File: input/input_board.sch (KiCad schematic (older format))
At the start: 21 parts, among them J2 SCKB, J4 SCKA, J5 MCLK, J6 SDOB1, U1 DS90LV048, U2 FIN1047, U5 74LVC541A

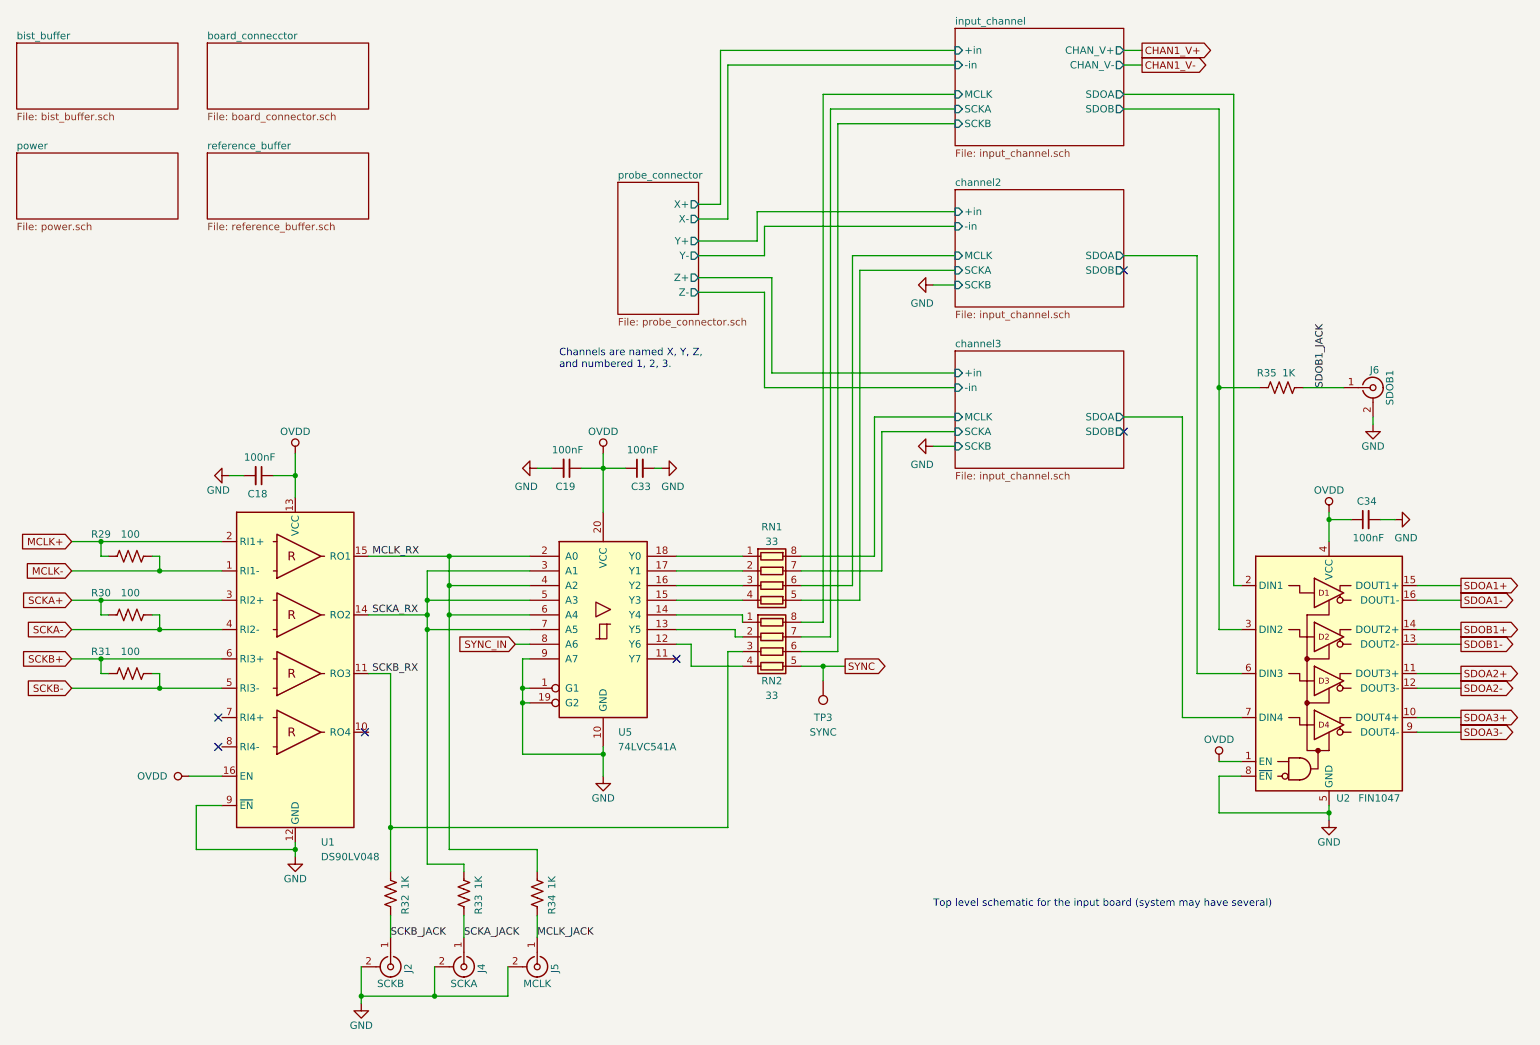
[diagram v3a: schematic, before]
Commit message: Input board is nearly ready to send off for the first spin.
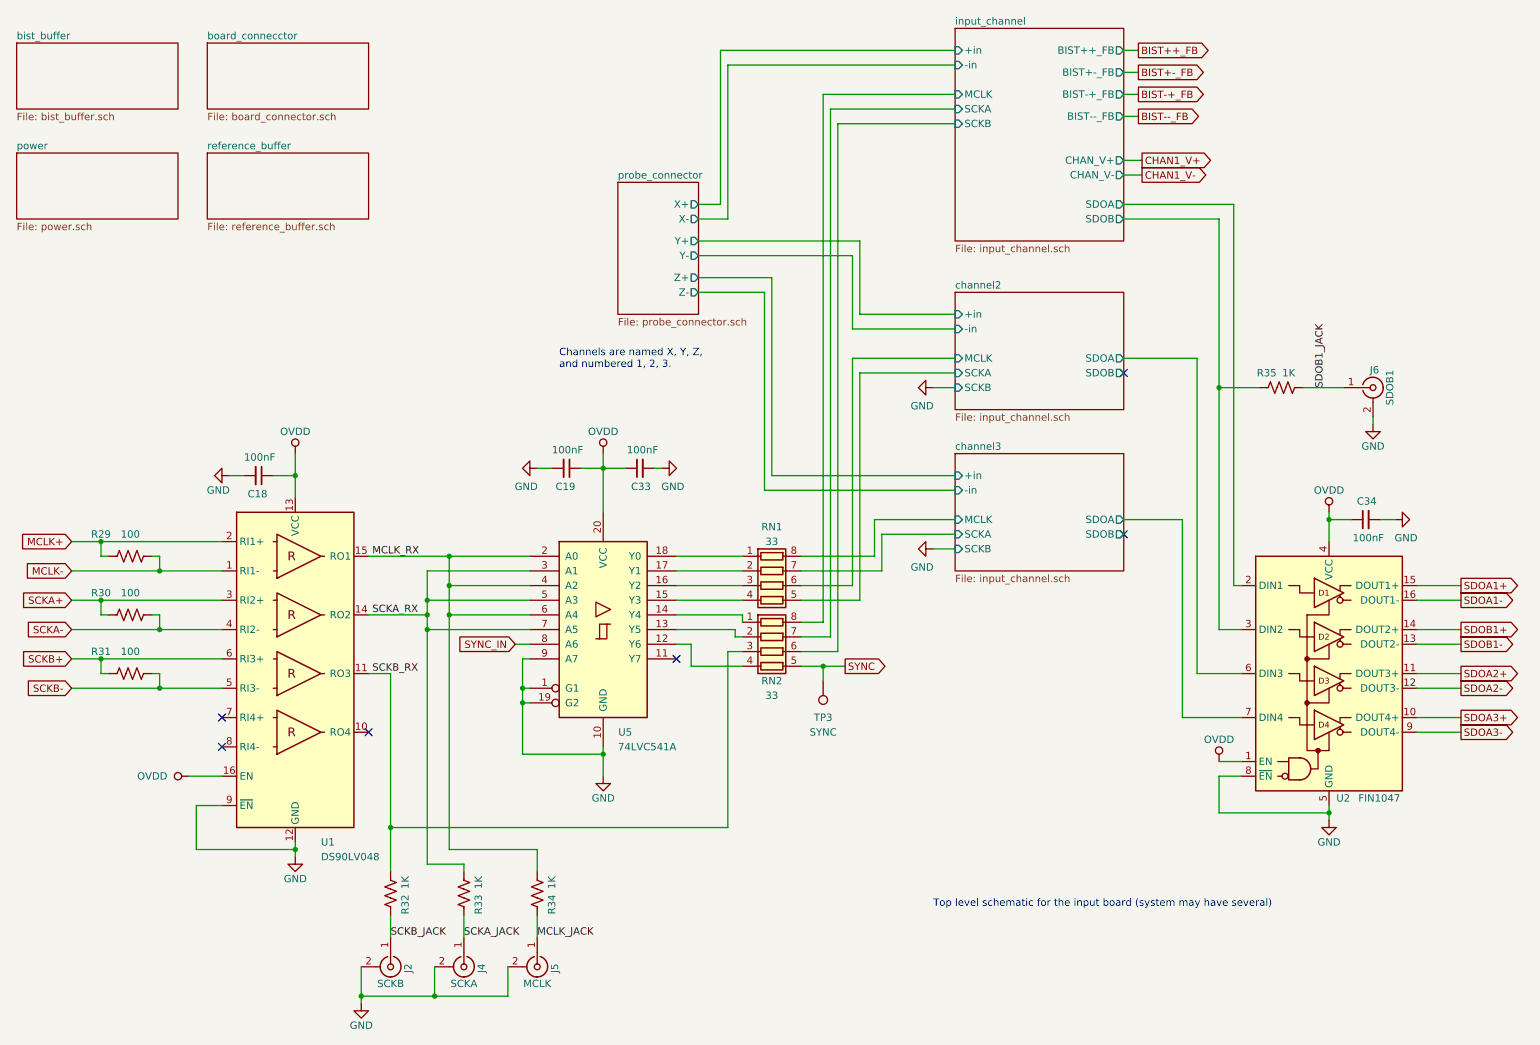
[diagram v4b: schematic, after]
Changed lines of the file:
@@
 $EndComp
-$Sheet
-S 7300 850  1150 800
-U 5DFCF14D
-F0 "input_channel" 50
-F1 "input_channel.sch" 50
-F2 "+in" I L 7300 1000 50
-F3 "-in" I L 7300 1100 50
-F4 "SDOA" O R 8450 1300 50
-F5 "SDOB" O R 8450 1400 50
-F6 "MCLK" I L 7300 1300 50
-F7 "SCKB" I L 7300 1500 50
-F8 "SCKA" I L 7300 1400 50
-F9 "CHAN_V+" O R 8450 1000 50
-F10 "CHAN_V-" O R 8450 1100 50
-$EndSheet
 $Sheet
 S 2200 950  1100 450
@@
 Text GLabel 6550 5200 2    50   Output ~ 0
 SYNC
-NoConn ~ 3275 5650
-NoConn ~ 2275 5750
-NoConn ~ 2275 5550
+NoConn ~ 3300 5650
+NoConn ~ 2300 5750
+NoConn ~ 2300 5550
 Text Notes 7150 6850 0    50   ~ 0
 Top level schematic for the input board (system may have several)
@@
 $EndSheet
 Wire Wire Line
-	8450 1300 9200 1300
-Wire Wire Line
-	9200 1300 9200 4650
-Wire Wire Line
 	9200 4650 9250 4650
 Wire Wire Line
-	8450 1400 9100 1400
-Wire Wire Line
-	9100 1400 9100 3300
-Wire Wire Line
 	9100 4950 9250 4950
 Wire Wire Line
 	9250 5250 8950 5250
 Wire Wire Line
-	8950 5250 8950 2400
-Wire Wire Line
-	8950 2400 8450 2400
+	8950 5250 8950 3100
 Wire Wire Line
 	9250 5550 8850 5550
 Wire Wire Line
-	8850 5550 8850 3500
-Wire Wire Line
-	8850 3500 8450 3500
-NoConn ~ 8450 2500
+	8850 5550 8850 4200
+NoConn ~ 8450 3200
 Wire Wire Line
 	5550 2050 5700 2050
@@
 	5700 2050 5700 1000
 Wire Wire Line
-	5700 1000 7300 1000
-Wire Wire Line
 	5750 2150 5750 1100
 Wire Wire Line
-	5750 1100 7300 1100
-Wire Wire Line
 	5550 2150 5750 2150
 Wire Wire Line
-	5550 2300 5950 2300
-Wire Wire Line
-	5950 2300 5950 2100
-Wire Wire Line
-	5950 2100 7300 2100
-Wire Wire Line
-	5550 2400 6000 2400
-Wire Wire Line
-	6000 2400 6000 2200
-Wire Wire Line
-	6000 2200 7300 2200
-Wire Wire Line
 	5550 2550 6050 2550
 Wire Wire Line
-	6050 2550 6050 3200
-Wire Wire Line
-	6050 3200 7300 3200
-Wire Wire Line
 	5550 2650 6000 2650
-Wire Wire Line
-	6000 2650 6000 3300
-Wire Wire Line
-	6000 3300 7300 3300
 $Comp
 L power:GND #PWR0131
@@
 L power:GND #PWR0147
 U 1 1 5E2F0AE0
-P 7150 3700
-F 0 "#PWR0147" H 7150 3450 50  0001 C CNN
-F 1 "GND" V 7275 3625 50  0000 C CNN
-F 2 "" H 7150 3700 50  0001 C CNN
-F 3 "" H 7150 3700 50  0001 C CNN
-	1    7150 3700
+P 7150 4400
+F 0 "#PWR0147" H 7150 4150 50  0001 C CNN
+F 1 "GND" V 7275 4325 50  0000 C CNN
+F 2 "" H 7150 4400 50  0001 C CNN
+F 3 "" H 7150 4400 50  0001 C CNN
+	1    7150 4400
 	0    1    1    0
 $EndComp
@@
 L power:GND #PWR0146
 U 1 1 5E2EC6DB
-P 7150 2600
-F 0 "#PWR0146" H 7150 2350 50  0001 C CNN
-F 1 "GND" V 7275 2525 50  0000 C CNN
-F 2 "" H 7150 2600 50  0001 C CNN
-F 3 "" H 7150 2600 50  0001 C CNN
-	1    7150 2600
+P 7150 3300
+F 0 "#PWR0146" H 7150 3050 50  0001 C CNN
+F 1 "GND" V 7275 3225 50  0000 C CNN
+F 2 "" H 7150 3300 50  0001 C CNN
+F 3 "" H 7150 3300 50  0001 C CNN
+	1    7150 3300
 	0    1    1    0
 $EndComp
 Wire Wire Line
-	7150 2600 7300 2600
-Wire Wire Line
-	7150 3700 7300 3700
-Wire Wire Line
-	7300 1300 6400 1300
-Wire Wire Line
-	7300 1400 6450 1400
-Wire Wire Line
-	7300 1500 6500 1500
+	7150 3300 7300 3300
+Wire Wire Line
+	7150 4400 7300 4400
 Wire Wire Line
 	5400 4450 5850 4450
@@
 	3450 5250 3450 6300
 Wire Wire Line
-	7300 2400 6600 2400
-Wire Wire Line
-	7300 2500 6650 2500
-Wire Wire Line
-	7300 3500 6750 3500
-Wire Wire Line
-	6750 3500 6750 4450
-Wire Wire Line
-	7300 3600 6800 3600
-Wire Wire Line
 	6400 4900 6250 4900
 Wire Wire Line
@@
 	6600 4650 6250 4650
 Wire Wire Line
-	6600 2400 6600 4650
-Wire Wire Line
 	6650 4750 6250 4750
 Wire Wire Line
-	6650 2500 6650 4750
-Wire Wire Line
 	6250 4450 6750 4450
 Wire Wire Line
 	6250 4550 6800 4550
-Wire Wire Line
-	6800 3600 6800 4550
 Text Label 3450 7050 0    50   ~ 0
 SCKB_JACK
@@
 Text Label 9825 3300 1    50   ~ 0
 SDOB1_JACK
-Text GLabel 8575 1000 2    50   Output ~ 0
+Text GLabel 8575 1750 2    50   Output ~ 0
 CHAN1_V+
-Text GLabel 8575 1100 2    50   Output ~ 0
+Text GLabel 8575 1850 2    50   Output ~ 0
 CHAN1_V-
 Wire Wire Line
-	8575 1000 8450 1000
-Wire Wire Line
-	8575 1100 8450 1100
+	8575 1750 8450 1750
+Wire Wire Line
+	8575 1850 8450 1850
 Text Notes 4600 3175 0    50   ~ 0
 Channels are named X, Y, Z,\nand numbered 1, 2, 3.
+NoConn ~ 8450 4300
 $Sheet
-S 7300 1950 1150 800
+S 7300 850  1150 1450
+U 5DFCF14D
+F0 "input_channel" 50
+F1 "input_channel.sch" 50
+F2 "+in" I L 7300 1000 50
+F3 "-in" I L 7300 1100 50
+F4 "SDOA" O R 8450 2050 50
+F5 "SDOB" O R 8450 2150 50
+F6 "MCLK" I L 7300 1300 50
+F7 "SCKB" I L 7300 1500 50
+F8 "SCKA" I L 7300 1400 50
+F9 "CHAN_V+" O R 8450 1750 50
+F10 "CHAN_V-" O R 8450 1850 50
+F11 "BIST-+_FB" O R 8450 1300 50
+F12 "BIST--_FB" O R 8450 1450 50
+F13 "BIST++_FB" O R 8450 1000 50
+F14 "BIST+-_FB" O R 8450 1150 50
+$EndSheet
+Wire Wire Line
+	8450 2050 9200 2050
+Wire Wire Line
+	9200 2050 9200 4650
+Wire Wire Line
+	8450 2150 9100 2150
+Wire Wire Line
+	9100 2150 9100 3300
+Wire Wire Line
+	8450 4200 8850 4200
+$Sheet
+S 7300 2650 1150 800
 U 5E448095
 F0 "channel2" 50
 F1 "input_channel.sch" 50
-F2 "+in" I L 7300 2100 50
-F3 "-in" I L 7300 2200 50
-F4 "SDOA" O R 8450 2400 50
-F5 "SDOB" O R 8450 2500 50
-F6 "MCLK" I L 7300 2400 50
-F7 "SCKB" I L 7300 2600 50
-F8 "SCKA" I L 7300 2500 50
+F2 "+in" I L 7300 2800 50
+F3 "-in" I L 7300 2900 50
+F4 "SDOA" O R 8450 3100 50
+F5 "SDOB" O R 8450 3200 50
+F6 "MCLK" I L 7300 3100 50
+F7 "SCKB" I L 7300 3300 50
+F8 "SCKA" I L 7300 3200 50
 $EndSheet
+Wire Wire Line
+	8450 3100 8950 3100
+Wire Wire Line
+	7300 1500 6500 1500
+Wire Wire Line
+	7300 1400 6450 1400
+Wire Wire Line
+	7300 1300 6400 1300
+Wire Wire Line
+	7300 1000 5700 1000
+Wire Wire Line
+	7300 1100 5750 1100
+Wire Wire Line
+	7300 3200 6650 3200
+Wire Wire Line
+	6650 3200 6650 4750
+Wire Wire Line
+	7300 3100 6600 3100
+Wire Wire Line
+	6600 3100 6600 4650
+Wire Wire Line
+	7300 4200 6750 4200
+Wire Wire Line
+	6750 4200 6750 4450
 $Sheet
-S 7300 3050 1150 800
+S 7300 3750 1150 800
 U 5E45936E
 F0 "channel3" 50
 F1 "input_channel.sch" 50
-F2 "+in" I L 7300 3200 50
-F3 "-in" I L 7300 3300 50
-F4 "SDOA" O R 8450 3500 50
-F5 "SDOB" O R 8450 3600 50
-F6 "MCLK" I L 7300 3500 50
-F7 "SCKB" I L 7300 3700 50
-F8 "SCKA" I L 7300 3600 50
+F2 "+in" I L 7300 3900 50
+F3 "-in" I L 7300 4000 50
+F4 "SDOA" O R 8450 4200 50
+F5 "SDOB" O R 8450 4300 50
+F6 "MCLK" I L 7300 4200 50
+F7 "SCKB" I L 7300 4400 50
+F8 "SCKA" I L 7300 4300 50
 $EndSheet
-NoConn ~ 8450 3600
+Wire Wire Line
+	7300 4300 6800 4300
+Wire Wire Line
+	6800 4300 6800 4550
+Wire Wire Line
+	6050 3900 7300 3900
+Wire Wire Line
+	6050 2550 6050 3900
+Wire Wire Line
+	6000 4000 7300 4000
+Wire Wire Line
+	6000 2650 6000 4000
+Wire Wire Line
+	6600 2400 6600 2900
+Wire Wire Line
+	6600 2900 7300 2900
+Wire Wire Line
+	5550 2400 6600 2400
+Wire Wire Line
+	6650 2300 6650 2800
+Wire Wire Line
+	6650 2800 7300 2800
+Wire Wire Line
+	5550 2300 6650 2300
+Text GLabel 8550 1300 2    50   Output ~ 0
+BIST-+_FB
+Text GLabel 8550 1450 2    50   Output ~ 0
+BIST--_FB
+Text GLabel 8550 1000 2    50   Output ~ 0
+BIST++_FB
+Text GLabel 8550 1150 2    50   Output ~ 0
+BIST+-_FB
+Wire Wire Line
+	8550 1450 8450 1450
+Wire Wire Line
+	8550 1300 8450 1300
+Wire Wire Line
+	8550 1150 8450 1150
+Wire Wire Line
+	8550 1000 8450 1000
 $EndSCHEMATC

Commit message: Fixed footprints for U5 and RN1/RN2.  Added gerber files for input board.  Start of work on the main board.
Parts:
- RN1, RN2: footprint Resistor_SMD:R_Array_Convex_4x1206 -> Resistor_SMD:R_Array_Convex_4x0603
- U5: footprint Package_SO:SSOP-20_4.4x6.5mm_P0.65mm -> input:my-SSOP-20_5.3x7.2mm_P0.65mm
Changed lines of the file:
@@
 F 0 "RN2" V 6250 5100 50  0000 C CNN
 F 1 "33" V 6350 5100 50  0000 C CNN
-F 2 "Resistor_SMD:R_Array_Convex_4x1206" V 6325 5100 50  0001 C CNN
+F 2 "Resistor_SMD:R_Array_Convex_4x0603" V 6325 5100 50  0001 C CNN
 F 3 "https://www.bourns.com/docs/Product-Datasheets/CATCAY.pdf" H 6050 5100 50  0001 C CNN
 F 4 "13" H 6050 5100 50  0001 C CNN "DK line"
@@
 F 0 "RN1" V 5650 4650 50  0000 C CNN
 F 1 "33" V 5750 4650 50  0000 C CNN
-F 2 "Resistor_SMD:R_Array_Convex_4x1206" V 6325 4650 50  0001 C CNN
+F 2 "Resistor_SMD:R_Array_Convex_4x0603" V 6325 4650 50  0001 C CNN
 F 3 "https://www.bourns.com/docs/Product-Datasheets/CATCAY.pdf" H 6050 4650 50  0001 C CNN
 F 4 "13" H 6050 4650 50  0001 C CNN "DK line"
@@
 F 0 "U5" H 5050 4250 50  0000 C CNN
 F 1 "74LVC541A" H 5200 4150 50  0000 C CNN
-F 2 "Package_SO:SSOP-20_4.4x6.5mm_P0.65mm" H 4900 4950 50  0001 C CNN
+F 2 "input:my-SSOP-20_5.3x7.2mm_P0.65mm" H 4900 4950 50  0001 C CNN
 F 3 "http://www.ti.com/lit/gpn/sn74LS541" H 4900 4950 50  0001 C CNN
 F 4 "11" H 4900 4950 50  0001 C CNN "DK line"

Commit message: Checkpoint of state before I start schematic revisions for the next version of the input board. There are not any substantive modifications to the input board, but some broad changes in component attributes related enabling a fabrication quote.
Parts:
- C18, C19, C33, C34: MPN (none) -> CC0603KRX7R8BB104; Manufacturer (none) -> Yageo
- J2, J4, J5, J6, TP3: Description (none) -> Do Not Populate; MPN (none) -> DNP
- R29, R30, R31: MPN (none) -> ERA-3AEB101V; Manufacturer (none) -> Panasonic Electronic Components
- R32, R33, R34, R35: MPN (none) -> ERA-3AEB102V; Manufacturer (none) -> Panasonic Electronic Components
- RN1, RN2: MPN (none) -> CAY16-330J4LF; Manufacturer (none) -> Bourns Inc.
- U1: MPN (none) -> DS90LV048ATMTC/NOPB; Manufacturer (none) -> Texas Instruments
- U2: MPN (none) -> FIN1047MTCX; Manufacturer (none) -> ON Semiconductor
- U5: MPN (none) -> SN74LVC541ADBR; Manufacturer (none) -> Texas Instruments
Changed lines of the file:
@@
 F 5 "0/4 Receiver  LVDS 16-TSSOP" H 2800 4650 50  0001 C CNN "Description"
 F 6 "DS90LV048ATMTC/NOPB-ND" H 2800 4650 50  0001 C CNN "Digikey"
+F 7 "DS90LV048ATMTC/NOPB" H 2800 4650 50  0001 C CNN "MPN"
+F 8 "Texas Instruments" H 2800 4650 50  0001 C CNN "Manufacturer"
 	1    2800 4650
 	1    0    0    -1
@@
 F 5 "FIN1047MTCXFSCT-ND" H 9850 5250 50  0001 C CNN "Digikey"
 F 6 "38" H 9850 5250 50  0001 C CNN "DK line"
+F 7 "FIN1047MTCX" H 9850 5250 50  0001 C CNN "MPN"
+F 8 "ON Semiconductor" H 9850 5250 50  0001 C CNN "Manufacturer"
 	1    9850 5250
 	1    0    0    -1
@@
 F 5 "RES ARRAY 4 RES 33 OHM 1206" H 6050 5100 50  0001 C CNN "Description"
 F 6 "CAY16-330J4LFCT-ND" H 6050 5100 50  0001 C CNN "Digikey"
+F 7 "CAY16-330J4LF" H 6050 5100 50  0001 C CNN "MPN"
+F 8 "Bourns Inc." H 6050 5100 50  0001 C CNN "Manufacturer"
 	1    6050 5100
 	0    1    1    0
@@
 F 5 "RES ARRAY 4 RES 33 OHM 1206" H 6050 4650 50  0001 C CNN "Description"
 F 6 "CAY16-330J4LFCT-ND" H 6050 4650 50  0001 C CNN "Digikey"
+F 7 "CAY16-330J4LF" H 6050 4650 50  0001 C CNN "MPN"
+F 8 "Bourns Inc." H 6050 4650 50  0001 C CNN "Manufacturer"
 	1    6050 4650
 	0    1    1    0
@@
 F 5 "51" H 1675 4450 50  0001 C CNN "DK line"
 F 6 "100 Ohms ±0.1% 0.1W, 1/10W Chip Resistor 0603 (1608 Metric) Automotive AEC-Q200 Thin Film" H 1675 4450 50  0001 C CNN "Description"
+F 7 "ERA-3AEB101V" H 1675 4450 50  0001 C CNN "MPN"
+F 8 "Panasonic Electronic Components" H 1675 4450 50  0001 C CNN "Manufacturer"
 	1    1675 4450
 	0    -1   -1   0
@@
 F 5 "51" H 1675 4850 50  0001 C CNN "DK line"
 F 6 "100 Ohms ±0.1% 0.1W, 1/10W Chip Resistor 0603 (1608 Metric) Automotive AEC-Q200 Thin Film" H 1675 4850 50  0001 C CNN "Description"
+F 7 "ERA-3AEB101V" H 1675 4850 50  0001 C CNN "MPN"
+F 8 "Panasonic Electronic Components" H 1675 4850 50  0001 C CNN "Manufacturer"
 	1    1675 4850
 	0    -1   -1   0
@@
 F 5 "51" H 1675 5250 50  0001 C CNN "DK line"
 F 6 "100 Ohms ±0.1% 0.1W, 1/10W Chip Resistor 0603 (1608 Metric) Automotive AEC-Q200 Thin Film" H 1675 5250 50  0001 C CNN "Description"
+F 7 "ERA-3AEB101V" H 1675 5250 50  0001 C CNN "MPN"
+F 8 "Panasonic Electronic Components" H 1675 5250 50  0001 C CNN "Manufacturer"
 	1    1675 5250
 	0    -1   -1   0
@@
 F 5 "311-1341-1-ND" H 2550 3900 50  0001 C CNN "Digikey"
 F 6 "2" H 2550 3900 50  0001 C CNN "DK line"
+F 7 "CC0603KRX7R8BB104" H 2550 3900 50  0001 C CNN "MPN"
+F 8 "Yageo" H 2550 3900 50  0001 C CNN "Manufacturer"
 	1    2550 3900
 	0    1    1    0
@@
 F 5 "311-1341-1-ND" H 4650 3850 50  0001 C CNN "Digikey"
 F 6 "2" H 4650 3850 50  0001 C CNN "DK line"
+F 7 "CC0603KRX7R8BB104" H 4650 3850 50  0001 C CNN "MPN"
+F 8 "Yageo" H 4650 3850 50  0001 C CNN "Manufacturer"
 	1    4650 3850
 	0    1    1    0
@@
 F 5 "311-1341-1-ND" H 10100 4200 50  0001 C CNN "Digikey"
 F 6 "2" H 10100 4200 50  0001 C CNN "DK line"
+F 7 "CC0603KRX7R8BB104" H 10100 4200 50  0001 C CNN "MPN"
+F 8 "Yageo" H 10100 4200 50  0001 C CNN "Manufacturer"
 	1    10100 4200
 	0    -1   -1   0
@@
 F 5 "311-1341-1-ND" H 5150 3850 50  0001 C CNN "Digikey"
 F 6 "2" H 5150 3850 50  0001 C CNN "DK line"
+F 7 "CC0603KRX7R8BB104" H 5150 3850 50  0001 C CNN "MPN"
+F 8 "Yageo" H 5150 3850 50  0001 C CNN "Manufacturer"
 	1    5150 3850
 	0    -1   -1   0
@@
 F 3 " ~" H 3950 7250 50  0001 C CNN
 F 4 "35" H 3950 7250 50  0001 C CNN "DK line"
+F 5 "Do Not Populate" H 3950 7250 50  0001 C CNN "Description"
+F 6 "DNP" H 3950 7250 50  0001 C CNN "MPN"
 	1    3950 7250
 	0    1    1    0
@@
 F 5 "RES SMD 1K OHM 0.1% 1/10W 0603" H 3950 6750 50  0001 C CNN "Description"
 F 6 "P1.0KDBCT-ND" H 3950 6750 50  0001 C CNN "Digikey"
+F 7 "ERA-3AEB102V" H 3950 6750 50  0001 C CNN "MPN"
+F 8 "Panasonic Electronic Components" H 3950 6750 50  0001 C CNN "Manufacturer"
 	1    3950 6750
 	1    0    0    -1
@@
 F 3 " ~" H 4450 7250 50  0001 C CNN
 F 4 "35" H 4450 7250 50  0001 C CNN "DK line"
+F 5 "Do Not Populate" H 4450 7250 50  0001 C CNN "Description"
+F 6 "DNP" H 4450 7250 50  0001 C CNN "MPN"
 	1    4450 7250
 	0    1    1    0
@@
 F 3 " ~" H 10150 3300 50  0001 C CNN
 F 4 "35" H 10150 3300 50  0001 C CNN "DK line"
+F 5 "Do Not Populate" H 10150 3300 50  0001 C CNN "Description"
+F 6 "DNP" H 10150 3300 50  0001 C CNN "MPN"
 	1    10150 3300
 	1    0    0    -1
@@
 F 5 "RES SMD 1K OHM 0.1% 1/10W 0603" H 9525 3300 50  0001 C CNN "Description"
 F 6 "P1.0KDBCT-ND" H 9525 3300 50  0001 C CNN "Digikey"
+F 7 "ERA-3AEB102V" H 9525 3300 50  0001 C CNN "MPN"
+F 8 "Panasonic Electronic Components" H 9525 3300 50  0001 C CNN "Manufacturer"
 	1    9525 3300
 	0    -1   -1   0
@@
 F 2 "TestPoint:TestPoint_THTPad_D1.5mm_Drill0.7mm" H 6600 5300 50  0001 C CNN
 F 3 "~" H 6600 5300 50  0001 C CNN
+F 4 "Do Not Populate" H 6400 5300 50  0001 C CNN "Description"
+F 5 "DNP" H 6400 5300 50  0001 C CNN "MPN"
 	1    6400 5300
 	-1   0    0    1
@@
 F 5 "IC BUF NON-INVERT 3.6V 20SSOP" H 4900 4950 50  0001 C CNN "Description"
 F 6 "296-8518-1-ND" H 4900 4950 50  0001 C CNN "Digikey"
+F 7 "SN74LVC541ADBR" H 4900 4950 50  0001 C CNN "MPN"
+F 8 "Texas Instruments" H 4900 4950 50  0001 C CNN "Manufacturer"
 	1    4900 4950
 	1    0    0    -1
@@
 F 5 "RES SMD 1K OHM 0.1% 1/10W 0603" H 3450 6750 50  0001 C CNN "Description"
 F 6 "P1.0KDBCT-ND" H 3450 6750 50  0001 C CNN "Digikey"
+F 7 "ERA-3AEB102V" H 3450 6750 50  0001 C CNN "MPN"
+F 8 "Panasonic Electronic Components" H 3450 6750 50  0001 C CNN "Manufacturer"
 	1    3450 6750
 	1    0    0    -1
@@
 F 5 "RES SMD 1K OHM 0.1% 1/10W 0603" H 4450 6750 50  0001 C CNN "Description"
 F 6 "P1.0KDBCT-ND" H 4450 6750 50  0001 C CNN "Digikey"
+F 7 "ERA-3AEB102V" H 4450 6750 50  0001 C CNN "MPN"
+F 8 "Panasonic Electronic Components" H 4450 6750 50  0001 C CNN "Manufacturer"
 	1    4450 6750
 	1    0    0    -1
@@
 F 3 " ~" H 3450 7250 50  0001 C CNN
 F 4 "35" H 3450 7250 50  0001 C CNN "DK line"
+F 5 "Do Not Populate" H 3450 7250 50  0001 C CNN "Description"
+F 6 "DNP" H 3450 7250 50  0001 C CNN "MPN"
 	1    3450 7250
 	0    1    1    0
